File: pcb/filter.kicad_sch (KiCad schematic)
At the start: 21 parts, among them U5 TL074

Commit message: update vca
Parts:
- C10, C11, C6, C7, C8, C9: footprint (none) -> Capacitor_THT:C_Disc_D6.0mm_W2.5mm_P5.00mm
- D10, D5, D6, D7, D8, D9: footprint (none) -> Diode_THT:D_DO-35_SOD27_P7.62mm_Horizontal
- R24, R25, R26, R27, R28, R29: footprint (none) -> Resistor_THT:R_Axial_DIN0207_L6.3mm_D2.5mm_P10.16mm_Horizontal
- RV5: footprint (none) -> Potentiometer_THT:Potentiometer_Bourns_PTV112-4_Dual_Vertical
- RV6: footprint (none) -> Potentiometer_THT:Potentiometer_Bourns_PTV09A-1_Single_Vertical
- U5: footprint (none) -> Package_DIP:DIP-14_W7.62mm
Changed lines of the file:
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@@
 			)
 		)
-		(property "Footprint" ""
+		(property "Footprint" "Resistor_THT:R_Axial_DIN0207_L6.3mm_D2.5mm_P10.16mm_Horizontal"
 			(at 233.172 53.34 90)
 			(effects
@@
 			)
 		)
-		(property "Footprint" ""
+		(property "Footprint" "Diode_THT:D_DO-35_SOD27_P7.62mm_Horizontal"
 			(at 181.61 99.06 0)
 			(effects
@@
 			)
 		)
-		(property "Footprint" ""
+		(property "Footprint" "Potentiometer_THT:Potentiometer_Bourns_PTV112-4_Dual_Vertical"
 			(at 125.73 40.64 0)
 			(effects
@@
 			)
 		)
-		(property "Footprint" ""
+		(property "Footprint" "Diode_THT:D_DO-35_SOD27_P7.62mm_Horizontal"
 			(at 172.72 99.06 0)
 			(effects
@@
 			)
 		)
-		(property "Footprint" ""
+		(property "Footprint" "Potentiometer_THT:Potentiometer_Bourns_PTV112-4_Dual_Vertical"
 			(at 171.45 43.18 0)
 			(effects
@@
 			)
 		)
-		(property "Footprint" ""
+		(property "Footprint" "Diode_THT:D_DO-35_SOD27_P7.62mm_Horizontal"
 			(at 172.72 110.49 0)
 			(effects
@@
 			)
 		)
-		(property "Footprint" ""
+		(property "Footprint" "Diode_THT:D_DO-35_SOD27_P7.62mm_Horizontal"
 			(at 190.5 99.06 0)
 			(effects
@@
 			)
 		)
-		(property "Footprint" ""
+		(property "Footprint" "Capacitor_THT:C_Disc_D6.0mm_W2.5mm_P5.00mm"
 			(at 134.3152 50.8 0)
 			(effects
@@
 			)
 		)
-		(property "Footprint" ""
+		(property "Footprint" "Resistor_THT:R_Axial_DIN0207_L6.3mm_D2.5mm_P10.16mm_Horizontal"
 			(at 179.07 121.158 90)
 			(effects
@@
 			)
 		)
-		(property "Footprint" ""
+		(property "Footprint" "Resistor_THT:R_Axial_DIN0207_L6.3mm_D2.5mm_P10.16mm_Horizontal"
 			(at 83.312 45.72 90)
 			(effects
@@
 			)
 		)
-		(property "Footprint" ""
+		(property "Footprint" "Capacitor_THT:C_Disc_D6.0mm_W2.5mm_P5.00mm"
 			(at 181.3052 53.34 0)
 			(effects
@@
 			)
 		)
-		(property "Footprint" ""
+		(property "Footprint" "Capacitor_THT:C_Disc_D6.0mm_W2.5mm_P5.00mm"
 			(at 265.1252 120.65 0)
 			(effects
@@
 			)
 		)
-		(property "Footprint" ""
+		(property "Footprint" "Diode_THT:D_DO-35_SOD27_P7.62mm_Horizontal"
 			(at 181.61 110.49 0)
 			(effects
@@
 			)
 		)
-		(property "Footprint" ""
+		(property "Footprint" "Package_DIP:DIP-14_W7.62mm"
 			(at 152.4 40.64 0)
 			(effects
@@
 			)
 		)
-		(property "Footprint" ""
+		(property "Footprint" "Package_DIP:DIP-14_W7.62mm"
 			(at 105.41 38.1 0)
 			(effects
@@
 			)
 		)
-		(property "Footprint" ""
+		(property "Footprint" "Package_DIP:DIP-14_W7.62mm"
 			(at 181.61 77.47 0)
 			(effects
@@
 			)
 		)
-		(property "Footprint" ""
+		(property "Footprint" "Resistor_THT:R_Axial_DIN0207_L6.3mm_D2.5mm_P10.16mm_Horizontal"
 			(at 184.912 125.73 90)
 			(effects
@@
 			)
 		)
-		(property "Footprint" ""
+		(property "Footprint" "Capacitor_THT:C_Disc_D6.0mm_W2.5mm_P5.00mm"
 			(at 229.87 44.7548 0)
 			(effects
@@
 			)
 		)
-		(property "Footprint" ""
+		(property "Footprint" "Potentiometer_THT:Potentiometer_Bourns_PTV09A-1_Single_Vertical"
 			(at 217.17 77.47 0)
 			(effects
@@
 			)
 		)
-		(property "Footprint" ""
+		(property "Footprint" "Diode_THT:D_DO-35_SOD27_P7.62mm_Horizontal"
 			(at 190.5 110.49 0)
 			(effects
@@
 			)
 		)
-		(property "Footprint" ""
+		(property "Footprint" "Resistor_THT:R_Axial_DIN0207_L6.3mm_D2.5mm_P10.16mm_Horizontal"
 			(at 68.072 45.72 90)
 			(effects
@@
 			)
 		)
-		(property "Footprint" ""
+		(property "Footprint" "Resistor_THT:R_Axial_DIN0207_L6.3mm_D2.5mm_P10.16mm_Horizontal"
 			(at 77.47 39.878 90)
 			(effects
@@
 			)
 		)
-		(property "Footprint" ""
+		(property "Footprint" "Package_DIP:DIP-14_W7.62mm"
 			(at 254 106.68 0)
 			(effects
@@
 			)
 		)
-		(property "Footprint" ""
+		(property "Footprint" "Package_DIP:DIP-14_W7.62mm"
 			(at 199.39 43.18 0)
 			(effects
@@
 			)
 		)
-		(property "Footprint" ""
+		(property "Footprint" "Capacitor_THT:C_Disc_D6.0mm_W2.5mm_P5.00mm"
 			(at 64.77 37.1348 0)
 			(effects
@@
 			)
 		)
-		(property "Footprint" ""
+		(property "Footprint" "Capacitor_THT:C_Disc_D6.0mm_W2.5mm_P5.00mm"
 			(at 249.8852 120.65 0)
 			(effects

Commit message: Update rails, start to clean
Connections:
- net +2V5 renamed +9V
- net -2V5 renamed -9V
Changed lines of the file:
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@@
-	)
-	(symbol
-		(lib_id "power:+2V5")
-		(at 248.92 104.14 0)
-		(unit 1)
-		(exclude_from_sim no)
-		(in_bom yes)
-		(on_board yes)
-		(dnp no)
-		(fields_autoplaced yes)
-		(property "Reference" "#PWR017"
-			(at 248.92 107.95 0)
-			(effects
-				(font
-					(size 1.27 1.27)
-				)
-				(hide yes)
-			)
-		)
-		(property "Value" "+2V5"
-			(at 248.92 99.06 0)
-			(effects
-				(font
-					(size 1.27 1.27)
-				)
-			)
-		)
-		(property "Footprint" ""
-			(at 248.92 104.14 0)
-			(effects
-				(font
-					(size 1.27 1.27)
-				)
-				(hide yes)
-			)
-		)
-		(property "Datasheet" ""
-			(at 248.92 104.14 0)
-			(effects
-				(font
-					(size 1.27 1.27)
-				)
-				(hide yes)
-			)
-		)
-		(property "Description" "Power symbol creates a global label with name \"+2V5\""
-			(at 248.92 104.14 0)
-			(effects
-				(font
-					(size 1.27 1.27)
-				)
-				(hide yes)
-			)
-		)
-		(pin "1"
-		)
-		(instances
-			(project ""
-				(path "/37001b8c-4a9b-42a8-aa4a-87d2c21e2f25/76fa81f6-dd43-4ad7-9821-88a95eed3bea"
-					(reference "#PWR017")
-					(unit 1)
-				)
-			)
-		)
 	)
 	(symbol
@@
 				(path "/37001b8c-4a9b-42a8-aa4a-87d2c21e2f25/76fa81f6-dd43-4ad7-9821-88a95eed3bea"
 					(reference "D8")
-					(unit 1)
-				)
-			)
-		)
-	)
-	(symbol
-		(lib_id "power:-2V5")
-		(at 264.16 104.14 0)
-		(unit 1)
-		(exclude_from_sim no)
-		(in_bom yes)
-		(on_board yes)
-		(dnp no)
-		(fields_autoplaced yes)
-		(property "Reference" "#PWR019"
-			(at 264.16 107.95 0)
-			(effects
-				(font
-					(size 1.27 1.27)
-				)
-				(hide yes)
-			)
-		)
-		(property "Value" "-2V5"
-			(at 264.16 99.06 0)
-			(effects
-				(font
-					(size 1.27 1.27)
-				)
-			)
-		)
-		(property "Footprint" ""
-			(at 264.16 104.14 0)
-			(effects
-				(font
-					(size 1.27 1.27)
-				)
-				(hide yes)
-			)
-		)
-		(property "Datasheet" ""
-			(at 264.16 104.14 0)
-			(effects
-				(font
-					(size 1.27 1.27)
-				)
-				(hide yes)
-			)
-		)
-		(property "Description" "Power symbol creates a global label with name \"-2V5\""
-			(at 264.16 104.14 0)
-			(effects
-				(font
-					(size 1.27 1.27)
-				)
-				(hide yes)
-			)
-		)
-		(pin "1"
-		)
-		(instances
-			(project ""
-				(path "/37001b8c-4a9b-42a8-aa4a-87d2c21e2f25/76fa81f6-dd43-4ad7-9821-88a95eed3bea"
-					(reference "#PWR019")
 					(unit 1)
 				)
@@
 	)
 	(symbol
+		(lib_id "power:+9V")
+		(at 248.92 104.14 0)
+		(unit 1)
+		(exclude_from_sim no)
+		(in_bom yes)
+		(on_board yes)
+		(dnp no)
+		(fields_autoplaced yes)
+		(property "Reference" "#PWR042"
+			(at 248.92 107.95 0)
+			(effects
+				(font
+					(size 1.27 1.27)
+				)
+				(hide yes)
+			)
+		)
+		(property "Value" "+9V"
+			(at 248.92 99.06 0)
+			(effects
+				(font
+					(size 1.27 1.27)
+				)
+			)
+		)
+		(property "Footprint" ""
+			(at 248.92 104.14 0)
+			(effects
+				(font
+					(size 1.27 1.27)
+				)
+				(hide yes)
+			)
+		)
+		(property "Datasheet" ""
+			(at 248.92 104.14 0)
+			(effects
+				(font
+					(size 1.27 1.27)
+				)
+				(hide yes)
+			)
+		)
+		(property "Description" "Power symbol creates a global label with name \"+9V\""
+			(at 248.92 104.14 0)
+			(effects
+				(font
+					(size 1.27 1.27)
+				)
+				(hide yes)
+			)
+		)
+		(pin "1"
+		)
+		(instances
+			(project ""
+				(path "/37001b8c-4a9b-42a8-aa4a-87d2c21e2f25/76fa81f6-dd43-4ad7-9821-88a95eed3bea"
+					(reference "#PWR042")
+					(unit 1)
+				)
+			)
+		)
+	)
+	(symbol
 		(lib_id "Device:C")
 		(at 226.06 45.72 90)
@@
 					(unit 1)
 				)
+			)
+		)
+	)
+	(symbol
+		(lib_id "power:-9V")
+		(at 264.16 104.14 0)
+		(unit 1)
+		(exclude_from_sim no)
+		(in_bom yes)
+		(on_board yes)
+		(dnp no)
+		(fields_autoplaced yes)
+		(property "Reference" "#PWR043"
+			(at 264.16 107.95 0)
+			(effects
+				(font
+					(size 1.27 1.27)
+				)
+				(hide yes)
+			)
+		)
+		(property "Value" "-9V"
+			(at 264.16 99.06 0)
+			(effects
+				(font
+					(size 1.27 1.27)
+				)
+			)
+		)
+		(property "Footprint" ""
+			(at 264.16 104.14 0)
+			(effects
+				(font
+					(size 1.27 1.27)
+				)
+				(hide yes)
+			)
+		)
+		(property "Datasheet" ""
+			(at 264.16 104.14 0)
+			(effects
+				(font
+					(size 1.27 1.27)
+				)
+				(hide yes)
+			)
+		)
+		(property "Description" "Power symbol creates a global label with name \"-9V\""
+			(at 264.16 104.14 0)
+			(effects
+				(font
+					(size 1.27 1.27)
+				)
+				(hide yes)
+			)
+		)
+		(pin "1"
+		)
+		(instances
+			(project ""
+				(path "/37001b8c-4a9b-42a8-aa4a-87d2c21e2f25/76fa81f6-dd43-4ad7-9821-88a95eed3bea"
+					(reference "#PWR043")
+					(unit 1)
+				)

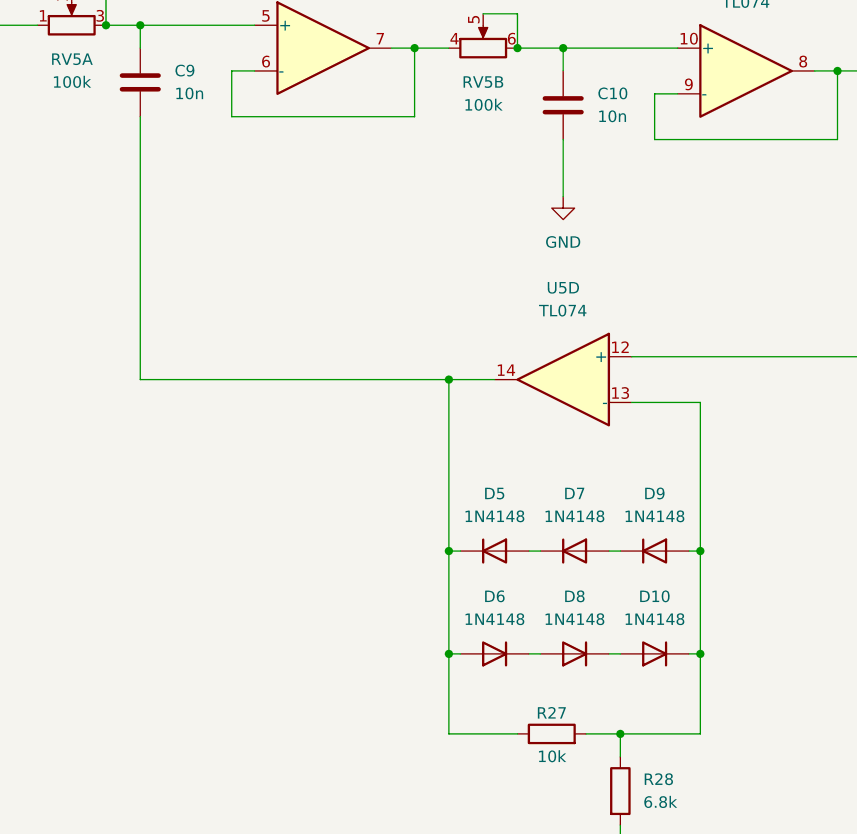
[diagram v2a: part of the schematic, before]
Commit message: Fix some labeling and DNP statues
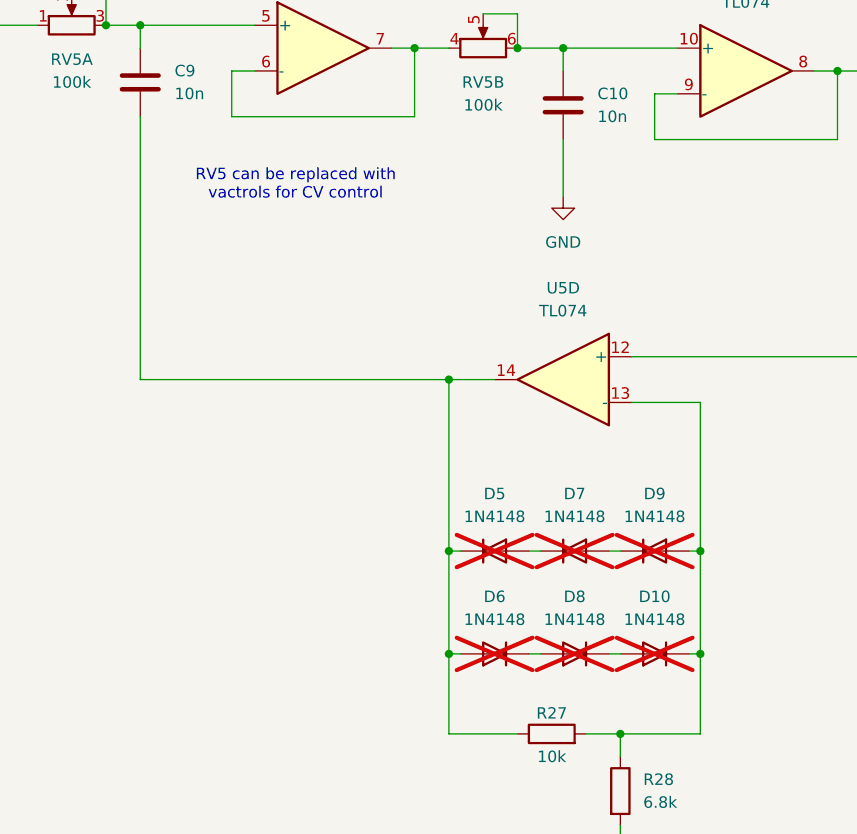
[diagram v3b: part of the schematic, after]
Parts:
- D10, D5, D6, D7, D8, D9: now not fitted
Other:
- note added: "RV5 can be replaced with vactrols for CV control"
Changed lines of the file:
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@@
+		)
+	)
+	(text "RV5 can be replaced with \nvactrols for CV control"
+		(exclude_from_sim no)
+		(at 150.622 58.42 0)
+		(effects
+			(font
+				(size 1.27 1.27)
+			)
 		)
 	)
@@
 		(in_bom yes)
 		(on_board yes)
-		(dnp no)
+		(dnp yes)
 		(fields_autoplaced yes)
 		(property "Reference" "D7"
@@
 		(in_bom yes)
 		(on_board yes)
-		(dnp no)
+		(dnp yes)
 		(fields_autoplaced yes)
 		(property "Reference" "D5"
@@
 		(in_bom yes)
 		(on_board yes)
-		(dnp no)
+		(dnp yes)
 		(fields_autoplaced yes)
 		(property "Reference" "D6"
@@
 		(in_bom yes)
 		(on_board yes)
-		(dnp no)
+		(dnp yes)
 		(fields_autoplaced yes)
 		(property "Reference" "D9"
@@
 		(in_bom yes)
 		(on_board yes)
-		(dnp no)
+		(dnp yes)
 		(fields_autoplaced yes)
 		(property "Reference" "D8"
@@
 		(in_bom yes)
 		(on_board yes)
-		(dnp no)
+		(dnp yes)
 		(fields_autoplaced yes)
 		(property "Reference" "D10"
